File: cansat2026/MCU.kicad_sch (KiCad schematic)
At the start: 42 parts, among them SW901 SW_SPST, U901 ESP32-S3-WROOM-1U-N4R8, U902 ESP32-S3-WROOM-1U-N4R8, U903 AW9523B, U904 PCA9306DQER, U905 PCA9306DQER

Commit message: ARLISSに作り直した
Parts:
- removed C903: 10uF, Capacitor_SMD:C_0402_1005Metric, symbol Device:C
- removed C904: 100nF, Capacitor_SMD:C_0402_1005Metric, symbol Device:C
- removed C905: 1uF, Capacitor_SMD:C_0402_1005Metric, symbol Device:C_Small
- removed C908, C909: 100nF, Capacitor_SMD:C_0402_1005Metric, symbol Device:C_Small
- removed R901: 10k, Resistor_SMD:R_0402_1005Metric, symbol Device:R_Small
- removed R905, R917: 10k, Resistor_SMD:R_0402_1005Metric, symbol Device:R
- removed R909: 4.7k, Resistor_SMD:R_0402_1005Metric, symbol Device:R
- removed R918, R923: 200k, Resistor_SMD:R_0402_1005Metric, symbol Device:R_Small
- removed R919: 150k, Resistor_SMD:R_0402_1005Metric, symbol Device:R
- removed U902: ESP32-S3-WROOM-1U-N4R8, PCM_Espressif:ESP32-S3-WROOM-1U, symbol PCM_Espressif:ESP32-S3-WROOM-1
- removed U904, U905: PCA9306DQER, Package_SON:X2SON-8_1.4x1mm_P0.35mm, symbol Interface:PCA9306D
- added R906, R907: 10k, Resistor_SMD:R_0402_1005Metric, symbol Device:R
- D901, D902, D903: LCSC Part C2286 -> (none)
- R908: value 4.7k -> 10k; LCSC Part C25900 -> C25744
- R912: renamed from R920; now not fitted
- R913: renamed from R921; now not fitted
- U901: LCSC Part C3013943 -> (none)
- renumbered C906 to C903, C907 to C904, R902 to R901, R903 to R902, R904 to R903, R906 to R904, R907 to R905, R911 to R909, R912 to R910, R913 to R911, R910 to R914, R924 to R915, R925 to R916, R914 to R917, R915 to R918, R916 to R919, U903 to U902
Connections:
- net CP_CAM_PIN_SIOC is gone; now on net CAM_PIN_SIOC: R912.2
- net CP_CAM_PIN_SIOD is gone; now on net CAM_PIN_SIOD: R913.2
- net I2C2SCL is gone; now on net FPGA_CDONE: U901.9 (GPIO16/U0CTS/ADC2_CH5/XTAL_32K_N)
- net FPGA_SPI_MISO: now also R908.2, U901.33 (MTDO/GPIO40/CLK_OUT2)
- net FPGA_SPI_MOSI: now also U901.32 (MTCK/GPIO39/CLK_OUT3/SUBSPICS1), R907.2
- net FPGA_SPI_SCK: now also U901.34 (MTDI/GPIO41/CLK_OUT1)
- net FPGA_SPI_SS: now also U901.35 (MTMS/GPIO42), R906.2
- net FPGA_~{CRESET}: now also U901.8 (GPIO15/U0RTS/ADC2_CH4/XTAL_32K_P)
- net MC1: now also U901.14 (GPIO20/U1CTS/ADC2_CH9/CLK_OUT1/USB_D+); no longer U901.34 (MTDI/GPIO41/CLK_OUT1)
- net MC2: now also U901.13 (GPIO19/U1RTS/ADC2_CH8/CLK_OUT2/USB_D-); no longer U901.35 (MTMS/GPIO42)
- net SW_SOFT: now also U901.12 (GPIO8/TOUCH8/ADC1_CH7/SUBSPICS1); no longer U901.31 (GPIO38/FSPIWP/SUBSPIWP)
- net VCC: now also R906.1, R907.1
- removed net I2C2SDA: R908.2, U901.8 (GPIO15/U0RTS/ADC2_CH4/XTAL_32K_P)
- net MCU_CAM_EN: no longer names the net of U902.10 (P0_4)
- no-connect marks 23 -> 10
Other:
- sheet FPGA ports: added CAM_PIN_PWDN, CAM_PIN_RESET, CAM_PIN_SIOC, CAM_PIN_SIOD; removed CP_CAM_PIN_D0, CP_CAM_PIN_D1, CP_CAM_PIN_D2, CP_CAM_PIN_D3, CP_CAM_PIN_D4, CP_CAM_PIN_D5, CP_CAM_PIN_D6, CP_CAM_PIN_D7, CP_CAM_PIN_HREF, CP_CAM_PIN_PCLK, CP_CAM_PIN_PWDN, CP_CAM_PIN_RESET, CP_CAM_PIN_VSYNC, LS_EN
- moved on the sheet: R904, R905, R914

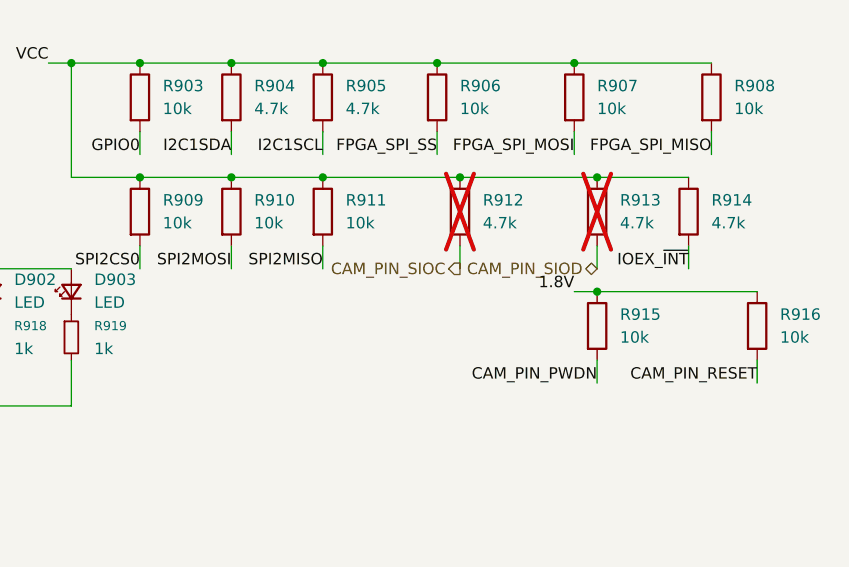
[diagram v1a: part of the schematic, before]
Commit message: カメラのSCCBのPUをDNPに
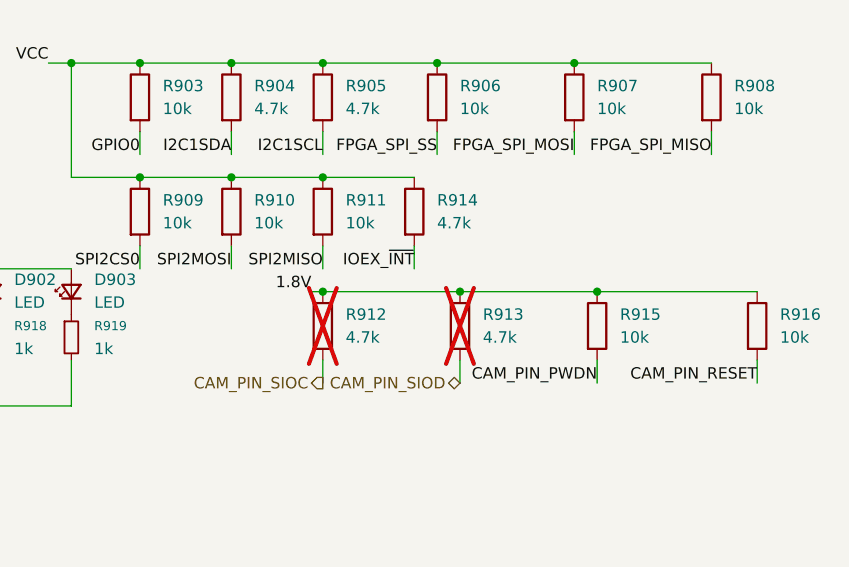
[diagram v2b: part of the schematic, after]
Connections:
- net 1.8V: now also R912.1, R913.1
- net VCC: no longer R912.1, R913.1
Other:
- moved on the sheet: R914
